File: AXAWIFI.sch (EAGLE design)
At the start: 24 parts, among them IC1 MCP2003, IC2 ESP12SMT, M1 REGMODULE4PIN, SW1 RESET, SW2 REFLASH

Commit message: Replaced voltage regulator module with K7833 for v1.1 release
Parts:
- removed M1: REGMODULE4PIN, freetronics-jon:REGMODULE4PIN
- added C1: 22uF 40V, analyzer:CPOL-USUD-6,3X5,8
- added REG1: K7833-500R3, freetronics-jon:K78XX-500R3
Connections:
- net +12V: now also REG1.IN; no longer M1.VIN+
- net 3.3V: now also C1.+, REG1.OUT; no longer M1.VOUT+
- net GND: now also C1.-, REG1.GND; no longer M1.VIN-, M1.VOUT-
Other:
- note added: "Copyright 2017-2018 SuperHouse Automation Pty Ltd Released under the terms of the TAPR Open Hardware License www.tapr.org/OHL"
- note added: "v1.1 (2018-06-25)"
- note removed: "Copyright 2017 SuperHouse Automation Pty Ltd Released under the terms of the TAPR Open Hardware License www.tapr.org/OHL"
- note removed: "NOTE: Pre-adjust vreg module to 3.3V before installation"
- note removed: "v1.0 (2017-06-04)"
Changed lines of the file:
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@@
 <?xml version="1.0" encoding="utf-8"?>
 <!DOCTYPE eagle SYSTEM "eagle.dtd">
-<eagle version="6.5.0">
+<eagle version="9.0.1">
 <drawing>
 <settings>
-<setting alwaysvectorfont="yes"/>
+<setting alwaysvectorfont="no"/>
+<setting keepoldvectorfont="yes"/>
 <setting verticaltext="up"/>
 </settings>
@@
 <layer number="60" name="p_dimension" color="6" fill="0" visible="no" active="no"/>
 <layer number="61" name="pt_docu" color="7" fill="0" visible="no" active="no"/>
+<layer number="88" name="SimResults" color="9" fill="1" visible="yes" active="yes"/>
+<layer number="89" name="SimProbes" color="9" fill="1" visible="yes" active="yes"/>
 <layer number="90" name="Modules" color="7" fill="1" visible="yes" active="yes"/>
 <layer number="91" name="Nets" color="2" fill="1" visible="yes" active="yes"/>
@@
 <part name="R10" library="freetronics-jon" deviceset="RESISTOR" device="0603" value="22K"/>
 <part name="R11" library="freetronics-jon" deviceset="RESISTOR" device="0603" value="22K"/>
-<part name="M1" library="freetronics-jon" deviceset="REGMODULE4PIN" device=""/>
 <part name="P+4" library="supply1" deviceset="+12V" device=""/>
 <part name="JP2" library="freetronics-jon" deviceset="M03" device="PTH"/>
@@
 <part name="R8" library="freetronics-jon" deviceset="RESISTOR" device="0603" value="10K"/>
 <part name="R12" library="freetronics-jon" deviceset="RESISTOR" device="0603" value="10K"/>
+<part name="REG1" library="freetronics-jon" deviceset="K78XX-500R3" device="" value="K7833-500R3"/>
+<part name="C1" library="analyzer" deviceset="CPOL-US" device="UD-6,3X5,8" value="22uF 40V"/>
 </parts>
 <sheets>
@@
 <plain>
 <text x="149.86" y="12.7" size="3.048" layer="94">AXA Window Motor WiFi Adapter</text>
-<text x="215.9" y="6.858" size="1.778" layer="94">v1.0 (2017-06-04)</text>
+<text x="215.9" y="6.858" size="1.778" layer="94">v1.1 (2018-06-25)</text>
 <text x="149.606" y="6.858" size="1.778" layer="94">superhouse.tv/axawifi</text>
 <text x="187.96" y="6.858" size="1.778" layer="94">SKU: AXAWIFI</text>
@@
 <frame x1="185.42" y1="5.08" x2="213.36" y2="10.16" columns="8" rows="5" layer="94"/>
 <frame x1="213.36" y1="5.08" x2="243.84" y2="10.16" columns="8" rows="5" layer="94"/>
-<text x="7.366" y="6.858" size="1.778" layer="94">Copyright 2017 SuperHouse Automation Pty Ltd
+<text x="7.366" y="6.858" size="1.778" layer="94">Copyright 2017-2018 SuperHouse Automation Pty Ltd
 Released under the terms of
 the TAPR Open Hardware License
@@
 <wire x1="139.7" y1="127" x2="245.11" y2="127" width="0.4064" layer="97" style="longdash"/>
 <wire x1="139.7" y1="127" x2="139.7" y2="181.61" width="0.4064" layer="97" style="longdash"/>
-<text x="157.48" y="129.54" size="1.778" layer="97">NOTE: Pre-adjust vreg module to 3.3V before installation</text>
 <text x="101.6" y="78.74" size="1.778" layer="94">GND</text>
 <text x="101.6" y="83.82" size="1.778" layer="94">3V3</text>
@@
 <instance part="R10" gate="G$1" x="172.72" y="78.74" rot="R90"/>
 <instance part="R11" gate="G$1" x="172.72" y="43.18" rot="R90"/>
-<instance part="M1" gate="G$1" x="185.42" y="162.56" rot="MR180"/>
 <instance part="P+4" gate="1" x="165.1" y="172.72"/>
 <instance part="JP2" gate="G$1" x="238.76" y="58.42" rot="R180"/>
@@
 <instance part="R8" gate="G$1" x="91.44" y="88.9" rot="R90"/>
 <instance part="R12" gate="G$1" x="91.44" y="43.18" rot="R90"/>
+<instance part="REG1" gate="G$1" x="182.88" y="167.64"/>
+<instance part="C1" gate="G$1" x="22.86" y="43.18" smashed="yes">
+<attribute name="NAME" x="23.876" y="44.323" size="1.778" layer="95"/>
+<attribute name="VALUE" x="18.796" y="36.449" size="1.778" layer="96" rot="R90"/>
+</instance>
 </instances>
 <busses>
@@
 <pinref part="JP4" gate="G$1" pin="2"/>
 <wire x1="213.36" y1="147.32" x2="213.36" y2="142.24" width="0.1524" layer="91"/>
-<wire x1="165.1" y1="142.24" x2="203.2" y2="142.24" width="0.1524" layer="91"/>
-<wire x1="203.2" y1="142.24" x2="213.36" y2="142.24" width="0.1524" layer="91"/>
+<wire x1="165.1" y1="142.24" x2="182.88" y2="142.24" width="0.1524" layer="91"/>
+<wire x1="182.88" y1="142.24" x2="213.36" y2="142.24" width="0.1524" layer="91"/>
 <wire x1="165.1" y1="142.24" x2="165.1" y2="139.7" width="0.1524" layer="91"/>
 <pinref part="GND13" gate="1" pin="GND"/>
@@
 <wire x1="226.06" y1="142.24" x2="213.36" y2="142.24" width="0.1524" layer="91"/>
 <junction x="213.36" y="142.24"/>
-<wire x1="200.66" y1="157.48" x2="203.2" y2="157.48" width="0.1524" layer="91"/>
-<wire x1="203.2" y1="157.48" x2="203.2" y2="142.24" width="0.1524" layer="91"/>
-<wire x1="165.1" y1="157.48" x2="170.18" y2="157.48" width="0.1524" layer="91"/>
-<wire x1="165.1" y1="157.48" x2="165.1" y2="142.24" width="0.1524" layer="91"/>
+<wire x1="165.1" y1="165.1" x2="165.1" y2="142.24" width="0.1524" layer="91"/>
 <junction x="165.1" y="142.24"/>
-<junction x="203.2" y="142.24"/>
-<pinref part="M1" gate="G$1" pin="VIN-"/>
-<pinref part="M1" gate="G$1" pin="VOUT-"/>
-<wire x1="165.1" y1="165.1" x2="165.1" y2="157.48" width="0.1524" layer="91"/>
-<junction x="165.1" y="157.48"/>
+<pinref part="REG1" gate="G$1" pin="GND"/>
+<wire x1="182.88" y1="160.02" x2="182.88" y2="142.24" width="0.1524" layer="91"/>
+<junction x="182.88" y="142.24"/>
 </segment>
 <segment>
@@
 <wire x1="121.92" y1="78.74" x2="121.92" y2="35.56" width="0.1524" layer="91"/>
 <junction x="121.92" y="35.56"/>
+<wire x1="81.28" y1="35.56" x2="22.86" y2="35.56" width="0.1524" layer="91"/>
+<pinref part="C1" gate="G$1" pin="-"/>
+<wire x1="22.86" y1="35.56" x2="22.86" y2="38.1" width="0.1524" layer="91"/>
 </segment>
 <segment>
@@
 <pinref part="C2" gate="G$1" pin="+"/>
 <pinref part="P+1" gate="G$1" pin="3.3V"/>
-<wire x1="200.66" y1="167.64" x2="213.36" y2="167.64" width="0.1524" layer="91"/>
+<wire x1="190.5" y1="167.64" x2="213.36" y2="167.64" width="0.1524" layer="91"/>
 <wire x1="213.36" y1="167.64" x2="226.06" y2="167.64" width="0.1524" layer="91"/>
 <pinref part="R5" gate="G$1" pin="2"/>
@@
 <wire x1="226.06" y1="165.1" x2="226.06" y2="167.64" width="0.1524" layer="91"/>
 <junction x="226.06" y="167.64"/>
-<pinref part="M1" gate="G$1" pin="VOUT+"/>
+<pinref part="REG1" gate="G$1" pin="OUT"/>
 </segment>
 <segment>
@@
 <wire x1="121.92" y1="83.82" x2="121.92" y2="106.68" width="0.1524" layer="91"/>
 <junction x="121.92" y="106.68"/>
+<pinref part="C1" gate="G$1" pin="+"/>
+<wire x1="22.86" y1="45.72" x2="22.86" y2="48.26" width="0.1524" layer="91"/>
+<junction x="22.86" y="48.26"/>
 </segment>
 </net>
@@
 <wire x1="157.48" y1="167.64" x2="165.1" y2="167.64" width="0.1524" layer="91"/>
 <pinref part="JP4" gate="G$1" pin="1"/>
-<wire x1="170.18" y1="167.64" x2="165.1" y2="167.64" width="0.1524" layer="91"/>
-<pinref part="M1" gate="G$1" pin="VIN+"/>
+<wire x1="175.26" y1="167.64" x2="165.1" y2="167.64" width="0.1524" layer="91"/>
 <pinref part="P+4" gate="1" pin="+12V"/>
 <wire x1="165.1" y1="167.64" x2="165.1" y2="170.18" width="0.1524" layer="91"/>
 <junction x="165.1" y="167.64"/>
-</segment>
-</net>
+<pinref part="REG1" gate="G$1" pin="IN"/>
+</segment>
+</net>

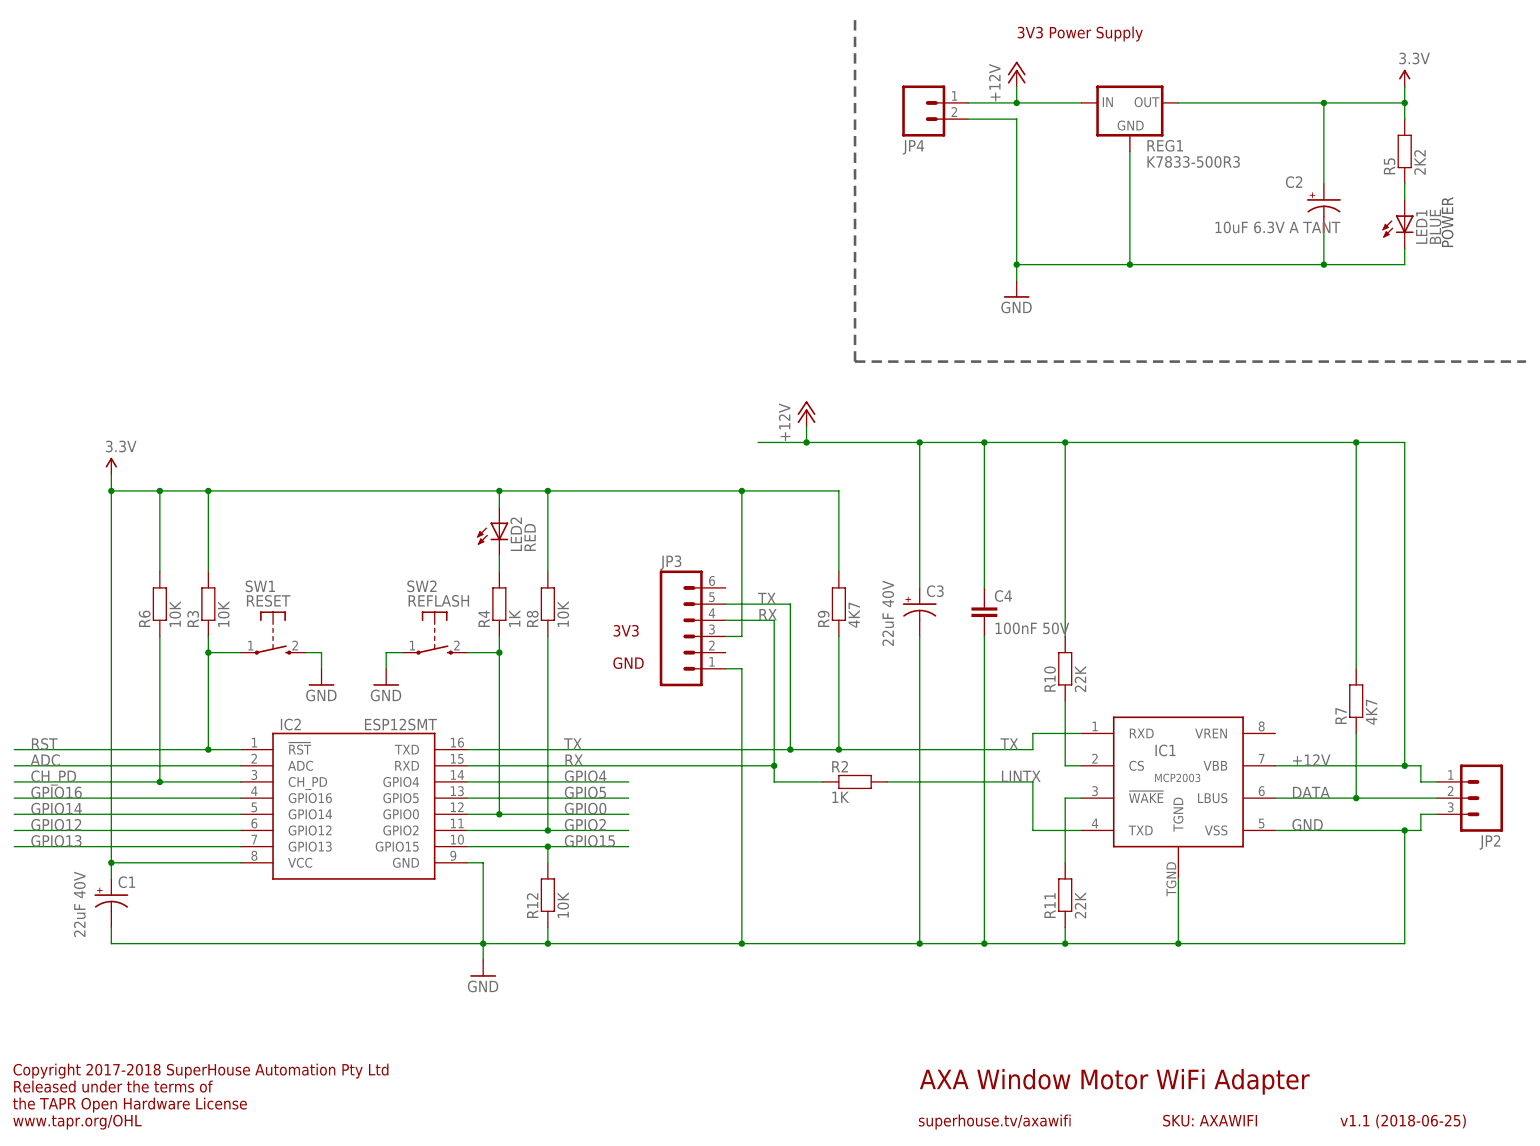
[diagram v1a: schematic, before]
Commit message: Replaced parts using SuperHouse library
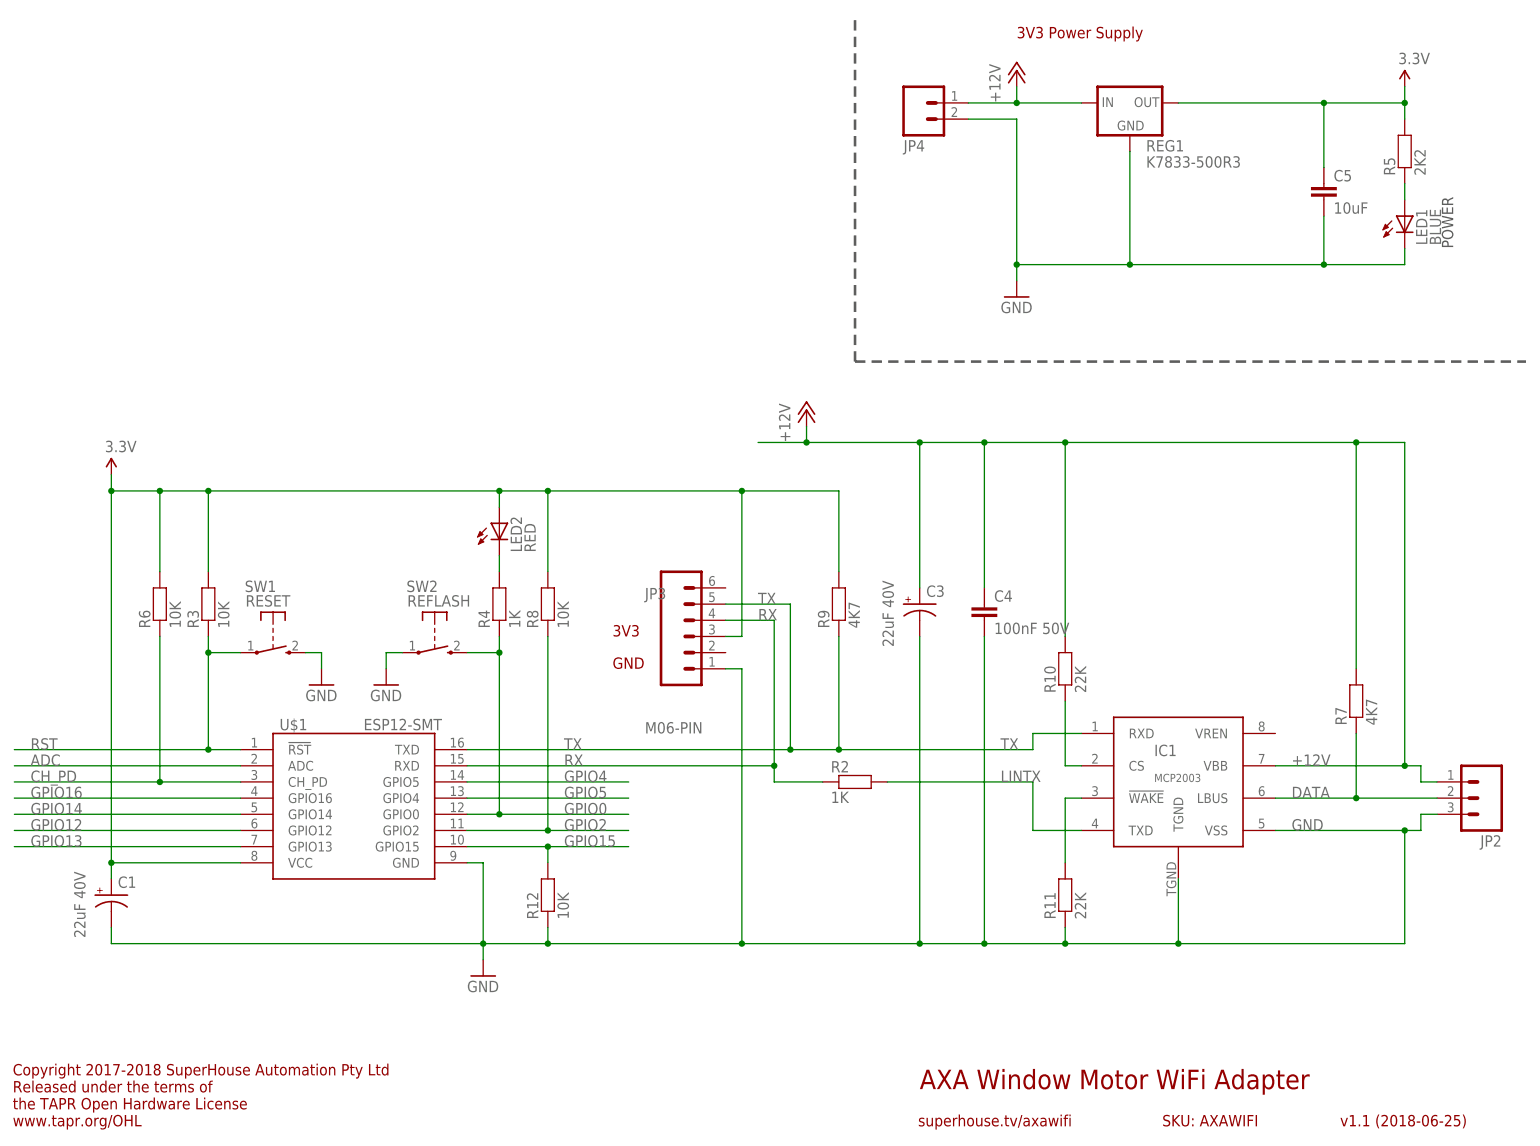
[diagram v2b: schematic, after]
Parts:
- removed C2: 10uF 6.3V A TANT, freetronics:CAP_POL1206
- removed IC2: ESP12SMT, freetronics-jon:ESP12SMT
- added C5: 10uF, SuperHouse-DiscreteSemi:CAP0805
- added U$1: ESP12-SMT, SuperHouse-MCUs:ESP12-SMT
- C4: device freetronics-jon:CAP0603 -> SuperHouse-DiscreteSemi:CAP0603
- JP3: value (none) -> M06-PIN; device freetronics-master-v1:M06SIP -> SuperHouse-Connectors:M06-PIN
- JP4: device freetronics-master-v1.1:M023.5MM -> SuperHouse-Connectors:M02-SCREW-3.5MM
- LED1, LED2: device freetronics-jon:LED0603 -> SuperHouse-LEDs:LED0603
- R10, R11, R12, R2, R3, R4, R5, R6, R7, R8, R9: device freetronics-jon:RESISTOR0603 -> SuperHouse-DiscreteSemi:RESISTOR0603
- REG1: device freetronics-jon:K78XX-500R3 -> SuperHouse-Regulators:K78XX-500R3
- SW1, SW2: device freetronics-jon:TAC_SWITCH_2PIN -> SuperHouse-Switches:TAC_SWITCH_2PINSMT
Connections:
- net 3.3V: now also C5.1, U$1.VCC; no longer C2.+, IC2.VCC
- net ADC: now also U$1.ADC; no longer IC2.ADC
- net CH_PD: now also U$1.CH_PD; no longer IC2.CH_PD
- net GND: now also C5.2, U$1.GND; no longer C2.-, IC2.GND
- net GPIO0: now also U$1.GPIO0; no longer IC2.GPIO0
- net GPIO12: now also U$1.GPIO12; no longer IC2.GPIO12
- net GPIO13: now also U$1.GPIO13; no longer IC2.GPIO13
- net GPIO14: now also U$1.GPIO14; no longer IC2.GPIO14
- net GPIO15: now also U$1.GPIO15; no longer IC2.GPIO15
- net GPIO16: now also U$1.GPIO16; no longer IC2.GPIO16
- net GPIO2: now also U$1.GPIO2; no longer IC2.GPIO2
- net GPIO4: now also U$1.GPIO5; no longer IC2.GPIO4
- net GPIO5: now also U$1.GPIO4; no longer IC2.GPIO5
- net RST: now also U$1.!RST; no longer IC2.!RST
- net RX: now also U$1.RXD; no longer IC2.RXD
- net TX: now also U$1.TXD; no longer IC2.TXD
